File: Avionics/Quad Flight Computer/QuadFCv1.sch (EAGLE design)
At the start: 111 parts, among them J1 10104111_MICROUSBAB, J2 1050270001, SW1 2-1437565-9, U1 TM4C123GH6PZ, U2 74LVC4245APW, U3 ATMEGA32U2-MU, U4 SPI_PPM, U5 MPU-6000, U6 HMC5883LSMD, U7 MS5611-01BA, U8 74AUP1G19GW, U9 S25FL127S, X1 HWB, Y1 32.768KHZ, Y2 AWSCR-20.00CW-T, Y3 PRQC16.00SR5010X000

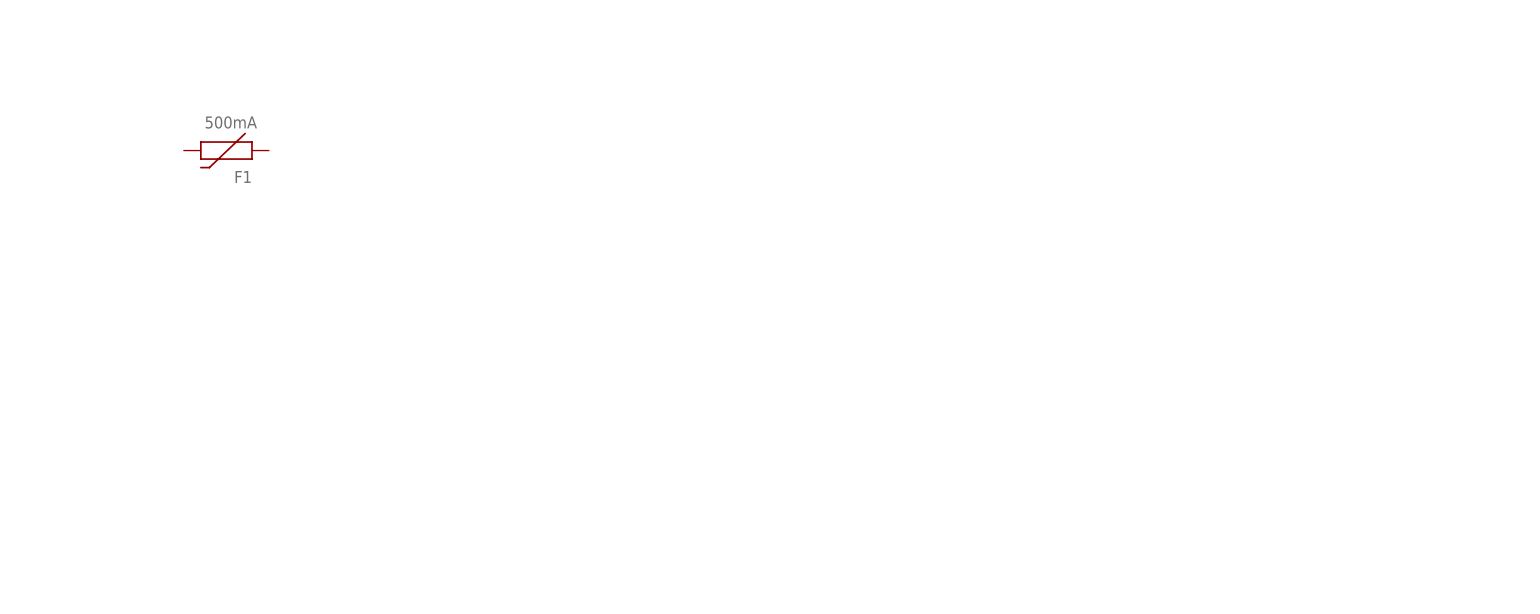
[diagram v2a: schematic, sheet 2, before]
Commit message: Added power management circuitry
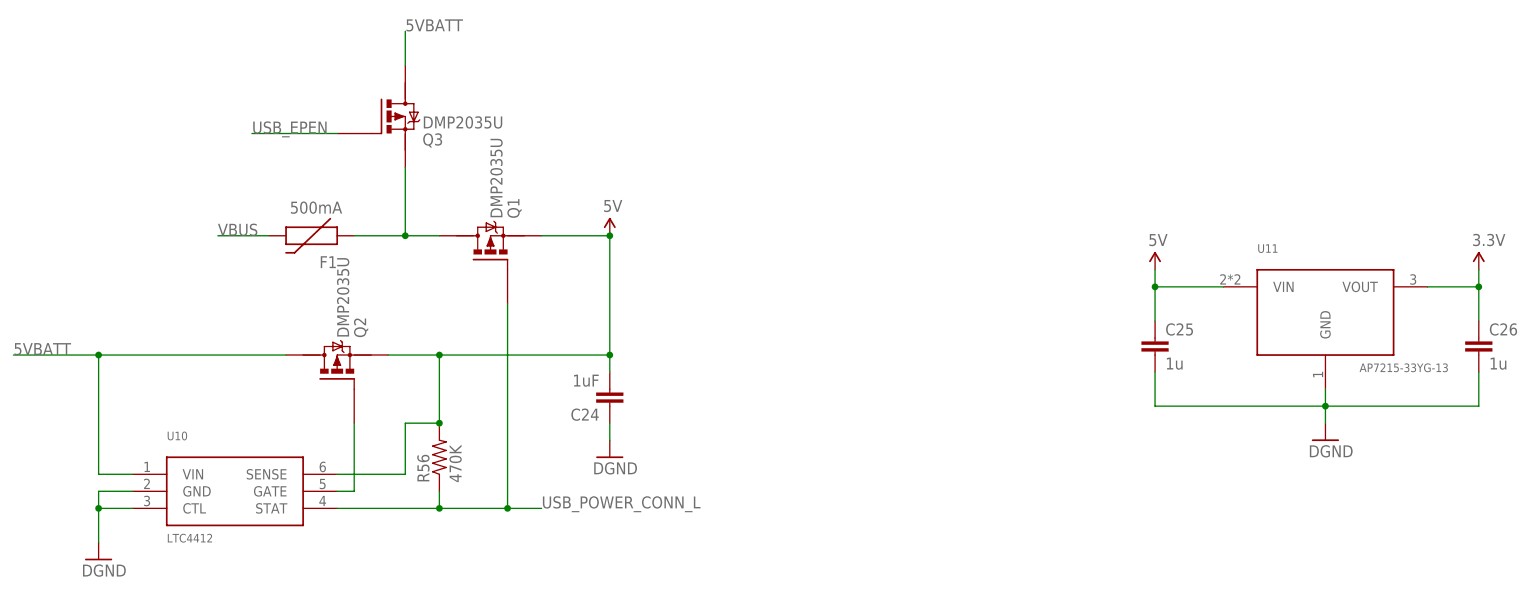
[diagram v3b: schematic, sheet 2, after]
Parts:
- added C24: 1uF, SparkFun-Capacitors:CAP0603-CAP
- added C25, C26: 1u, SparkFun-Capacitors:CAP0402-CAP
- added Q1, Q2, Q3: DMP2035U, Shared Libraries:DMP2035U
- added R56: 470K, Shared Libraries:RESISTOR0402-RES
- added U10: LTC4412, Shared Libraries:LTC4412
- added U11: AP7215-33YG-13, Shared Libraries:AP7215-33YG-13
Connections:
- new net N$41: Q2.G, U10.GATE
- new net N$42: F1.1, Q1.D, Q3.S
- new net USB_EPEN: Q3.G
- new net USB_POWER_CONN_L: Q1.G, R56.1, U10.STAT
- new net VBUS: F1.2
- net 3.3V: now also C26.1, U11.VOUT
- net 5V: now also C24.2, C25.1, Q1.S, Q2.S, R56.2, U10.SENSE, U11.VIN
- net 5VBATT: now also Q2.D, Q3.D, U10.VIN
- net GND: now also C24.1, C25.2, C26.2, U10.CTL, U10.GND, U11.GND
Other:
- moved on the sheet: F1
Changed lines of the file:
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@@
 <part name="SUPPLY5" library="SparkFun-Aesthetics" deviceset="5V" device=""/>
 <part name="R55" library="SparkFun-Resistors" deviceset="RESISTOR" device="0402-RES" value="0"/>
+<part name="Q1" library="Shared Libraries" deviceset="DMP2035U" device=""/>
+<part name="Q2" library="Shared Libraries" deviceset="DMP2035U" device=""/>
+<part name="Q3" library="Shared Libraries" deviceset="DMP2035U" device=""/>
+<part name="U10" library="Shared Libraries" deviceset="LTC4412" device=""/>
+<part name="R56" library="Shared Libraries" deviceset="RESISTOR" device="0402-RES" value="470K"/>
+<part name="C24" library="SparkFun-Capacitors" deviceset="CAP" device="0603-CAP" value="1uF"/>
+<part name="GND39" library="SparkFun-Aesthetics" deviceset="DGND" device=""/>
+<part name="GND40" library="SparkFun-Aesthetics" deviceset="DGND" device=""/>
+<part name="SUPPLY29" library="SparkFun-Aesthetics" deviceset="5V" device=""/>
+<part name="U11" library="Shared Libraries" deviceset="AP7215-33YG-13" device=""/>
+<part name="SUPPLY28" library="SparkFun-Aesthetics" deviceset="5V" device=""/>
+<part name="SUPPLY30" library="SparkFun-Aesthetics" deviceset="3.3V" device=""/>
+<part name="GND41" library="SparkFun-Aesthetics" deviceset="DGND" device=""/>
+<part name="C25" library="SparkFun-Capacitors" deviceset="CAP" device="0402-CAP" value="1u"/>
+<part name="C26" library="SparkFun-Capacitors" deviceset="CAP" device="0402-CAP" value="1u"/>
 </parts>
 <sheets>
@@
 </plain>
 <instances>
-<instance part="F1" gate="G$1" x="-2.54" y="0" rot="R180"/>
+<instance part="F1" gate="G$1" x="10.16" y="-12.7" rot="R180"/>
+<instance part="Q1" gate="G$1" x="35.56" y="-15.24" rot="MR90"/>
+<instance part="Q2" gate="G$1" x="12.7" y="-33.02" rot="MR90"/>
+<instance part="Q3" gate="G$1" x="20.32" y="5.08" rot="MR180"/>
+<instance part="U10" gate="G$1" x="-2.54" y="-50.8"/>
+<instance part="R56" gate="G$1" x="27.94" y="-45.72" rot="R90"/>
+<instance part="C24" gate="G$1" x="53.34" y="-35.56" rot="R180"/>
+<instance part="GND39" gate="G$1" x="-22.86" y="-60.96"/>
+<instance part="GND40" gate="G$1" x="53.34" y="-45.72"/>
+<instance part="SUPPLY29" gate="G$1" x="53.34" y="-12.7"/>
+<instance part="U11" gate="G$1" x="160.02" y="-25.4"/>
+<instance part="SUPPLY28" gate="G$1" x="134.62" y="-17.78"/>
+<instance part="SUPPLY30" gate="G$1" x="182.88" y="-17.78"/>
+<instance part="GND41" gate="G$1" x="160.02" y="-43.18"/>
+<instance part="C25" gate="G$1" x="134.62" y="-30.48"/>
+<instance part="C26" gate="G$1" x="182.88" y="-30.48"/>
 </instances>
 <busses>
 </busses>
 <nets>
+<net name="N$41" class="0">
+<segment>
+<pinref part="Q2" gate="G$1" pin="G"/>
+<wire x1="15.24" y1="-40.64" x2="15.24" y2="-50.8" width="0.1524" layer="91"/>
+<pinref part="U10" gate="G$1" pin="GATE"/>
+<wire x1="15.24" y1="-50.8" x2="12.7" y2="-50.8" width="0.1524" layer="91"/>
+</segment>
+</net>
+<net name="5VBATT" class="0">
+<segment>
+<pinref part="U10" gate="G$1" pin="VIN"/>
+<wire x1="-17.78" y1="-48.26" x2="-22.86" y2="-48.26" width="0.1524" layer="91"/>
+<wire x1="-22.86" y1="-48.26" x2="-22.86" y2="-30.48" width="0.1524" layer="91"/>
+<pinref part="Q2" gate="G$1" pin="D"/>
+<wire x1="-22.86" y1="-30.48" x2="5.08" y2="-30.48" width="0.1524" layer="91"/>
+<junction x="-22.86" y="-30.48"/>
+<wire x1="-22.86" y1="-30.48" x2="-35.56" y2="-30.48" width="0.1524" layer="91"/>
+<label x="-35.56" y="-30.48" size="1.778" layer="95"/>
+</segment>
+<segment>
+<pinref part="Q3" gate="G$1" pin="D"/>
+<wire x1="22.86" y1="12.7" x2="22.86" y2="17.78" width="0.1524" layer="91"/>
+<label x="22.86" y="17.78" size="1.778" layer="95"/>
+</segment>
+</net>
+<net name="USB_POWER_CONN_L" class="0">
+<segment>
+<pinref part="U10" gate="G$1" pin="STAT"/>
+<pinref part="Q1" gate="G$1" pin="G"/>
+<wire x1="12.7" y1="-53.34" x2="27.94" y2="-53.34" width="0.1524" layer="91"/>
+<wire x1="27.94" y1="-53.34" x2="38.1" y2="-53.34" width="0.1524" layer="91"/>
+<wire x1="38.1" y1="-53.34" x2="38.1" y2="-22.86" width="0.1524" layer="91"/>
+<pinref part="R56" gate="G$1" pin="1"/>
+<wire x1="27.94" y1="-50.8" x2="27.94" y2="-53.34" width="0.1524" layer="91"/>
+<junction x="27.94" y="-53.34"/>
+<wire x1="38.1" y1="-53.34" x2="43.18" y2="-53.34" width="0.1524" layer="91"/>
+<junction x="38.1" y="-53.34"/>
+<label x="43.18" y="-53.34" size="1.778" layer="95"/>
+</segment>
+</net>
+<net name="GND" class="0">
+<segment>
+<pinref part="U10" gate="G$1" pin="GND"/>
+<wire x1="-17.78" y1="-50.8" x2="-22.86" y2="-50.8" width="0.1524" layer="91"/>
+<wire x1="-22.86" y1="-50.8" x2="-22.86" y2="-53.34" width="0.1524" layer="91"/>
+<pinref part="U10" gate="G$1" pin="CTL"/>
+<wire x1="-22.86" y1="-53.34" x2="-22.86" y2="-58.42" width="0.1524" layer="91"/>
+<wire x1="-17.78" y1="-53.34" x2="-22.86" y2="-53.34" width="0.1524" layer="91"/>
+<junction x="-22.86" y="-53.34"/>
+<pinref part="GND39" gate="G$1" pin="GND"/>
+</segment>
+<segment>
+<pinref part="C24" gate="G$1" pin="1"/>
+<pinref part="GND40" gate="G$1" pin="GND"/>
+<wire x1="53.34" y1="-40.64" x2="53.34" y2="-43.18" width="0.1524" layer="91"/>
+</segment>
+<segment>
+<pinref part="GND41" gate="G$1" pin="GND"/>
+<wire x1="160.02" y1="-40.64" x2="160.02" y2="-38.1" width="0.1524" layer="91"/>
+<pinref part="C26" gate="G$1" pin="2"/>
+<wire x1="182.88" y1="-33.02" x2="182.88" y2="-38.1" width="0.1524" layer="91"/>
+<pinref part="U11" gate="G$1" pin="GND"/>
+<wire x1="182.88" y1="-38.1" x2="160.02" y2="-38.1" width="0.1524" layer="91"/>
+<wire x1="160.02" y1="-38.1" x2="160.02" y2="-35.56" width="0.1524" layer="91"/>
+<pinref part="C25" gate="G$1" pin="2"/>
+<wire x1="160.02" y1="-38.1" x2="134.62" y2="-38.1" width="0.1524" layer="91"/>
+<wire x1="134.62" y1="-38.1" x2="134.62" y2="-33.02" width="0.1524" layer="91"/>
+<junction x="160.02" y="-38.1"/>
+</segment>
+</net>
+<net name="5V" class="0">
+<segment>
+<pinref part="Q2" gate="G$1" pin="S"/>
+<wire x1="20.32" y1="-30.48" x2="27.94" y2="-30.48" width="0.1524" layer="91"/>
+<wire x1="27.94" y1="-30.48" x2="53.34" y2="-30.48" width="0.1524" layer="91"/>
+<wire x1="53.34" y1="-30.48" x2="53.34" y2="-12.7" width="0.1524" layer="91"/>
+<pinref part="Q1" gate="G$1" pin="S"/>
+<wire x1="53.34" y1="-12.7" x2="43.18" y2="-12.7" width="0.1524" layer="91"/>
+<pinref part="U10" gate="G$1" pin="SENSE"/>
+<wire x1="12.7" y1="-48.26" x2="22.86" y2="-48.26" width="0.1524" layer="91"/>
+<wire x1="22.86" y1="-48.26" x2="22.86" y2="-40.64" width="0.1524" layer="91"/>
+<pinref part="R56" gate="G$1" pin="2"/>
+<wire x1="22.86" y1="-40.64" x2="27.94" y2="-40.64" width="0.1524" layer="91"/>
+<wire x1="27.94" y1="-40.64" x2="27.94" y2="-30.48" width="0.1524" layer="91"/>
+<junction x="27.94" y="-40.64"/>
+<junction x="27.94" y="-30.48"/>
+<pinref part="SUPPLY29" gate="G$1" pin="5V"/>
+<junction x="53.34" y="-12.7"/>
+<pinref part="C24" gate="G$1" pin="2"/>
+<wire x1="53.34" y1="-33.02" x2="53.34" y2="-30.48" width="0.1524" layer="91"/>
+<junction x="53.34" y="-30.48"/>
+</segment>
+<segment>
+<pinref part="SUPPLY28" gate="G$1" pin="5V"/>
+<pinref part="C25" gate="G$1" pin="1"/>
+<wire x1="134.62" y1="-17.78" x2="134.62" y2="-20.32" width="0.1524" layer="91"/>
+<pinref part="U11" gate="G$1" pin="VIN"/>
+<wire x1="134.62" y1="-20.32" x2="134.62" y2="-25.4" width="0.1524" layer="91"/>
+<wire x1="144.78" y1="-20.32" x2="134.62" y2="-20.32" width="0.1524" layer="91"/>
+<junction x="134.62" y="-20.32"/>
+</segment>
+</net>
+<net name="USB_EPEN" class="0">
+<segment>
+<pinref part="Q3" gate="G$1" pin="G"/>
+<wire x1="12.7" y1="2.54" x2="0" y2="2.54" width="0.1524" layer="91"/>
+<label x="0" y="2.54" size="1.778" layer="95"/>
+</segment>
+</net>
+<net name="VBUS" class="0">
+<segment>
+<pinref part="F1" gate="G$1" pin="2"/>
+<wire x1="2.54" y1="-12.7" x2="-5.08" y2="-12.7" width="0.1524" layer="91"/>
+<label x="-5.08" y="-12.7" size="1.778" layer="95"/>
+</segment>
+</net>
+<net name="N$42" class="0">
+<segment>
+<pinref part="F1" gate="G$1" pin="1"/>
+<pinref part="Q1" gate="G$1" pin="D"/>
+<wire x1="15.24" y1="-12.7" x2="22.86" y2="-12.7" width="0.1524" layer="91"/>
+<pinref part="Q3" gate="G$1" pin="S"/>
+<wire x1="22.86" y1="-12.7" x2="27.94" y2="-12.7" width="0.1524" layer="91"/>
+<wire x1="22.86" y1="-2.54" x2="22.86" y2="-12.7" width="0.1524" layer="91"/>
+<junction x="22.86" y="-12.7"/>
+</segment>
+</net>
+<net name="3.3V" class="0">
+<segment>
+<pinref part="U11" gate="G$1" pin="VOUT"/>
+<pinref part="SUPPLY30" gate="G$1" pin="3.3V"/>
+<wire x1="175.26" y1="-20.32" x2="182.88" y2="-20.32" width="0.1524" layer="91"/>
+<wire x1="182.88" y1="-20.32" x2="182.88" y2="-17.78" width="0.1524" layer="91"/>
+<pinref part="C26" gate="G$1" pin="1"/>
+<wire x1="182.88" y1="-20.32" x2="182.88" y2="-25.4" width="0.1524" layer="91"/>
+<junction x="182.88" y="-20.32"/>
+</segment>
+</net>
 </nets>
 </sheet>
@@
 <wire x1="22.86" y1="-129.54" x2="22.86" y2="-132.08" width="0.1524" layer="91"/>
 <wire x1="17.78" y1="-129.54" x2="22.86" y2="-129.54" width="0.1524" layer="91"/>
+<junction x="22.86" y="-129.54"/>
 </segment>
 </net>
@@
 </sheet>
 </sheets>
+<errors>
+</errors>
 </schematic>
 </drawing>
